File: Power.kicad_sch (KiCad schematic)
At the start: 49 parts, among them SW901 DP3T, U901 BQ24075, U902 TPS7A0533PDBV, U903 LP5907MFX-3.3

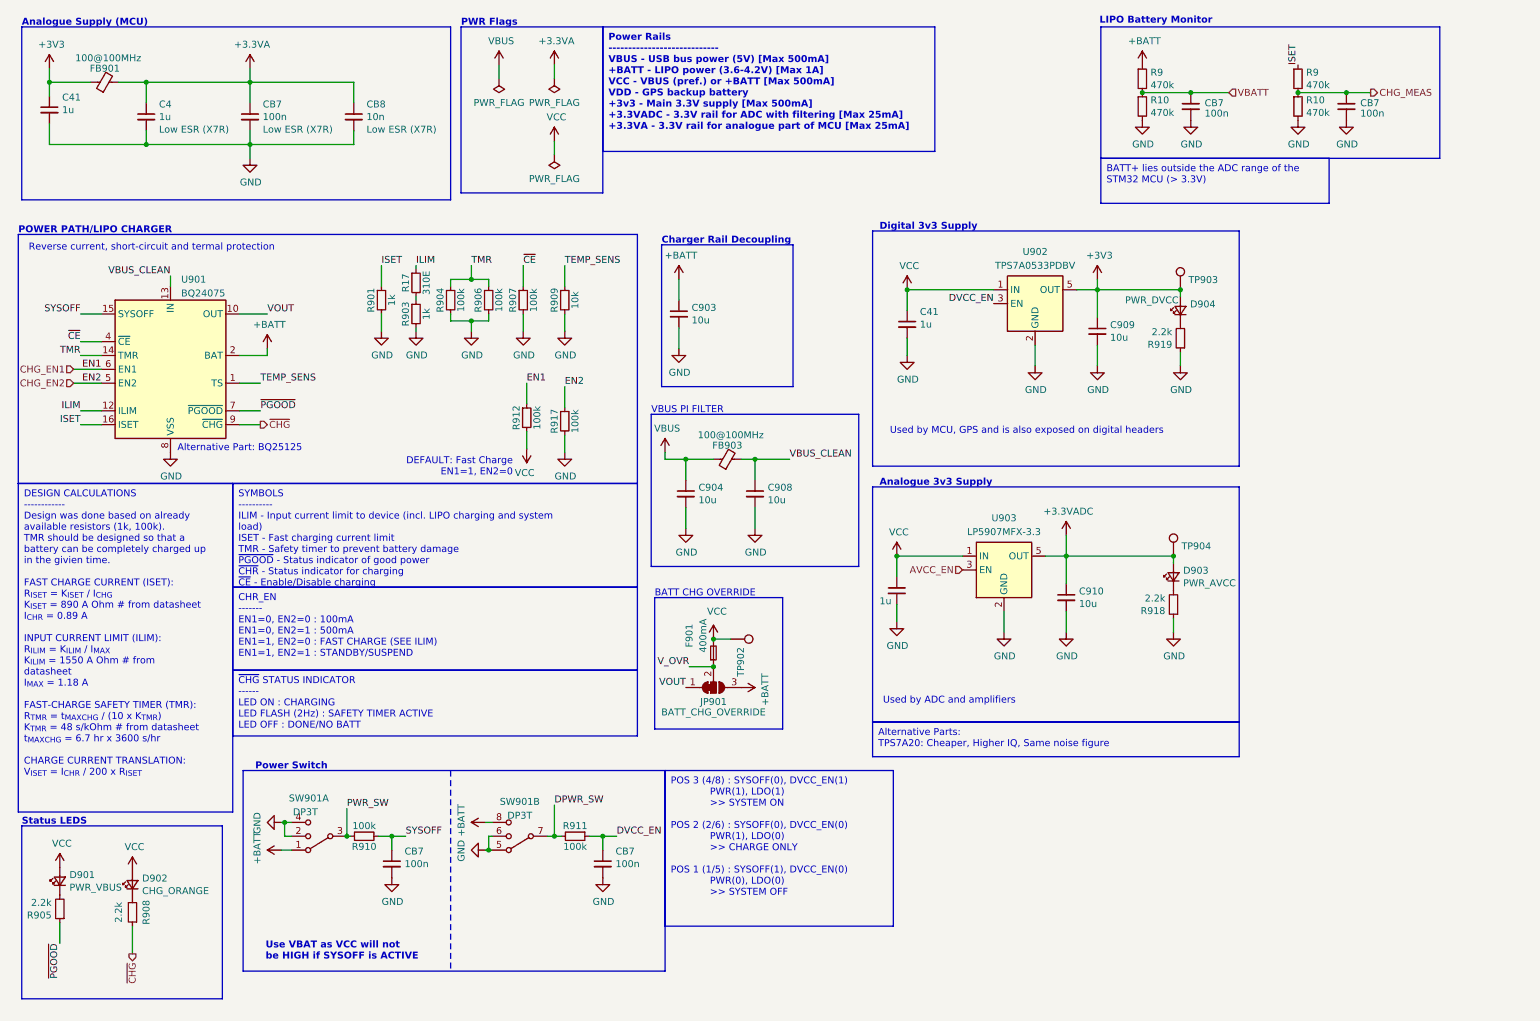
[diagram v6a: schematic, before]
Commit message: (sch) add analogue VCC load switch
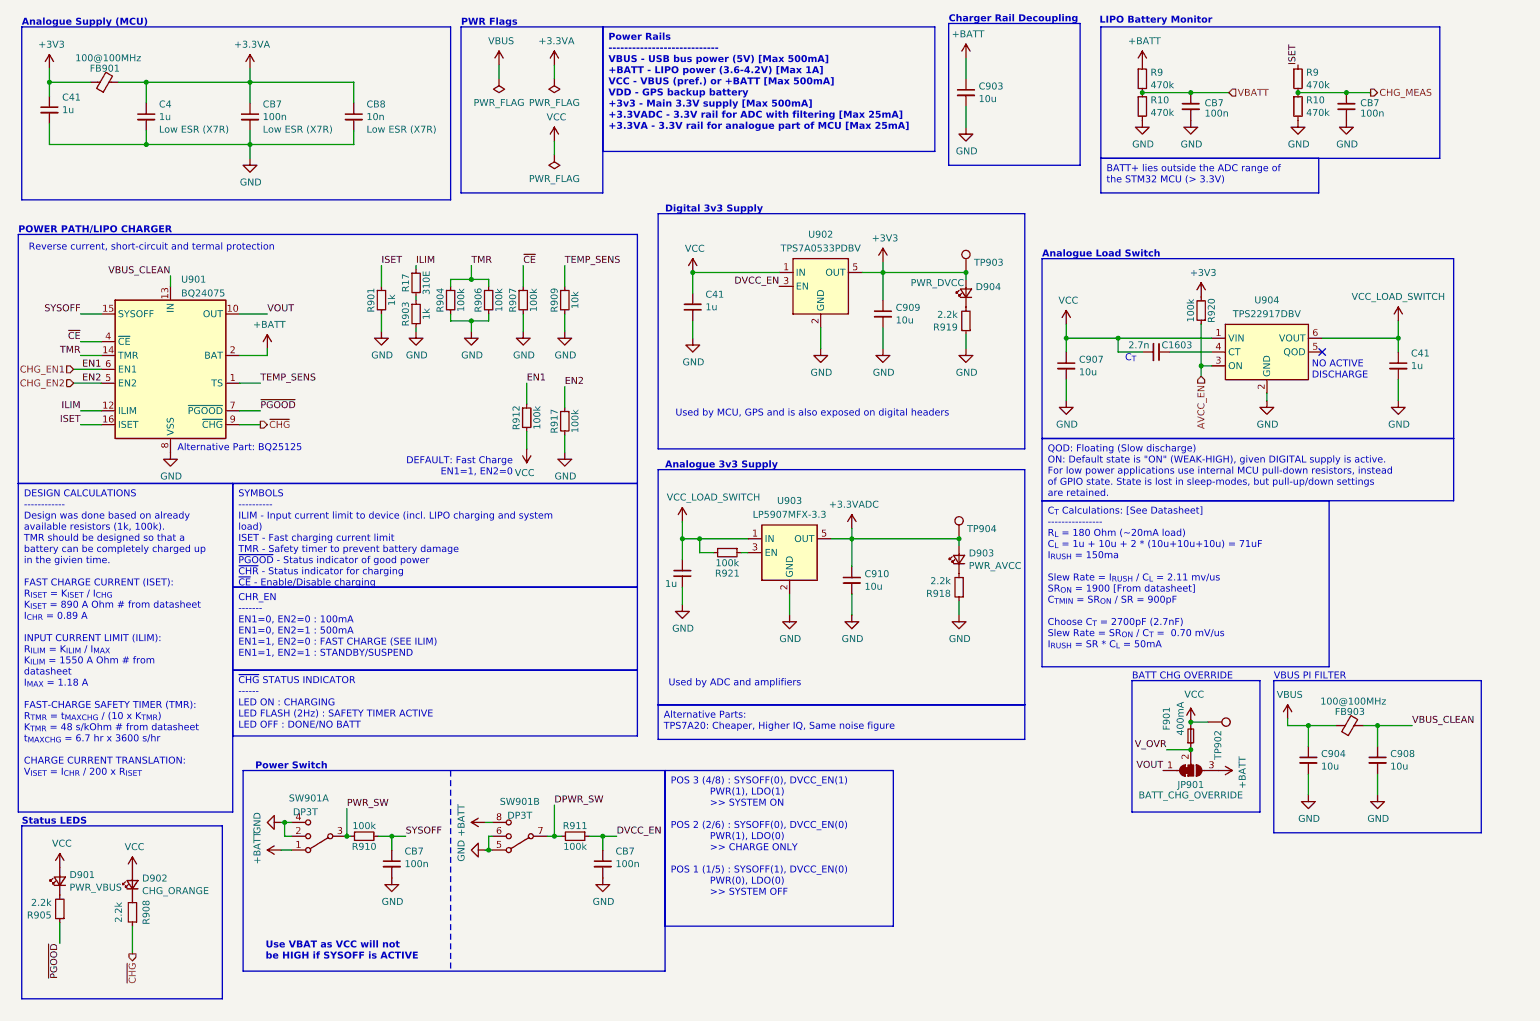
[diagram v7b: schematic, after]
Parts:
- added C1603: 2.7n, Capacitor_SMD:C_0402_1005Metric, symbol Device:C_Small
- added C41: 1u, Capacitor_SMD:C_0402_1005Metric, symbol Device:C_Small
- added C907: 10u, Capacitor_SMD:C_0402_1005Metric, symbol Device:C_Small
- added R920, R921: 100k, Resistor_SMD:R_0402_1005Metric, symbol Device:R_Small
- added U904: TPS22917DBV, Package_TO_SOT_SMD:SOT-23-6, symbol Power_Management:TPS22917DBV
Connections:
- net +3V3: now also R920.2
- net AVCC_EN: now also R920.1, U904.3 (ON); no longer U903.3 (EN)
- net GND: now also C41.2, C907.2, U904.2 (GND)
- net VCC: now also C1603.2, C907.1, U904.1 (VIN); no longer C41.1, U903.1 (IN)
- new net: C1603.1, U904.4 (CT)
- new net: R921.1, U903.3 (EN)
- new net VCC_LOAD_SWITCH: C41.1, C41.1, R921.2, U903.1 (IN), U904.6 (VOUT)
- no-connect marks 0 -> 1
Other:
- note added: "Analogue Load Switch"
- note added: "C_{T}"
- note added: "NO ACTIVE DISCHARGE"
- moved on the sheet: C41, C903, C904, C908, C909, C910, D903, D904, F901, FB903, JP901, R918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

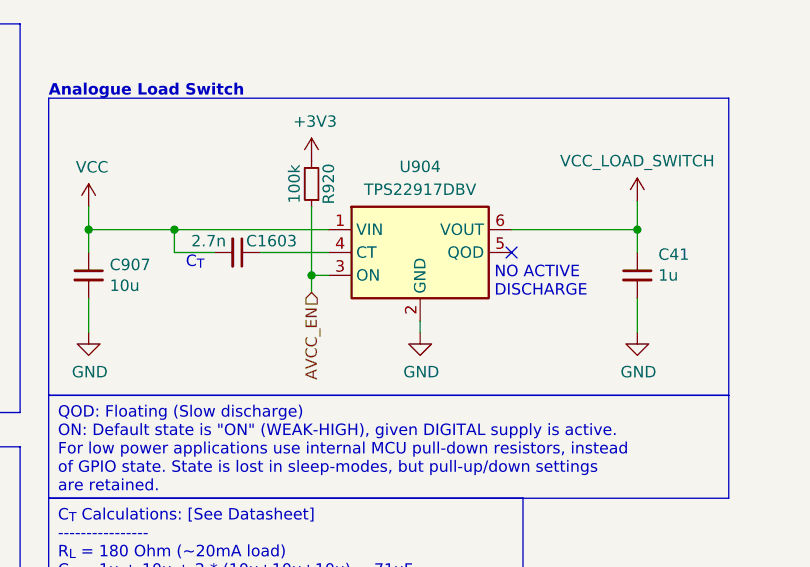
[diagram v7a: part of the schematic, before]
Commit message: (pcb) initial load switch layout
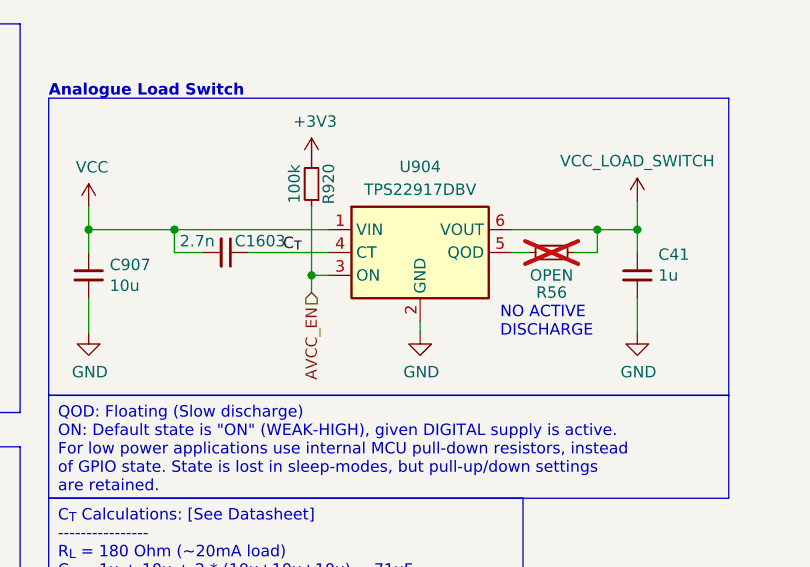
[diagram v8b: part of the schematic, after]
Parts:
- added R56: OPEN, Resistor_SMD:R_0402_1005Metric, symbol Device:R_Small
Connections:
- net VCC_LOAD_SWITCH: now also R56.2
- net C_{T}: now reaches C1603.1, U904.4 (CT)
- net at U904.5 (QOD): now also R56.1
- no-connect marks 1 -> 0
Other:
- note removed: "C_{T}"
- moved on the sheet: C1603
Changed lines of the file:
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@@
   (junction (at 267.97 73.66) (diameter 0) (color 0 0 0 0)
   )
+  (junction (at 263.525 73.66) (diameter 0) (color 0 0 0 0)
+  )
   (junction (at 121.92 165.1) (diameter 0) (color 0 0 0 0)
   )
@@
   (junction (at 139.7 110.49) (diameter 0) (color 0 0 0 0)
   )
-  (no_connect (at 254 76.2))
   (polyline (pts (xy 132.08 50.8) (xy 132.08 93.98))
     (stroke (width 0) (type default))
@@
     (stroke (width 0) (type default))
   )
-  (wire (pts (xy 226.06 76.2) (xy 233.68 76.2))
+  (wire (pts (xy 224.79 76.2) (xy 233.68 76.2))
     (stroke (width 0) (type default))
   )
@@
   )
   (wire (pts (xy 187.325 111.76) (xy 187.325 110.49))
+    (stroke (width 0) (type default))
+  )
+  (wire (pts (xy 254 76.2) (xy 255.905 76.2))
     (stroke (width 0) (type default))
   )
@@
     (stroke (width 0) (type default))
   )
-  (wire (pts (xy 220.98 76.2) (xy 216.535 76.2))
+  (wire (pts (xy 219.71 76.2) (xy 216.535 76.2))
     (stroke (width 0) (type default))
   )
@@
     (stroke (width 0) (type default))
   )
+  (wire (pts (xy 263.525 73.66) (xy 267.97 73.66))
+    (stroke (width 0) (type default))
+  )
+  (wire (pts (xy 260.985 76.2) (xy 263.525 76.2))
+    (stroke (width 0) (type default))
+  )
   (polyline (pts (xy 121.92 16.51) (xy 121.92 46.99))
     (stroke (width 0) (type default))
@@
     (stroke (width 0) (type default))
   )
+  (wire (pts (xy 263.525 76.2) (xy 263.525 73.66))
+    (stroke (width 0) (type default))
+  )
   (wire (pts (xy 136.525 110.49) (xy 139.7 110.49))
     (stroke (width 0) (type default))
@@
     (stroke (width 0) (type default))
   )
-  (wire (pts (xy 254 73.66) (xy 267.97 73.66))
+  (wire (pts (xy 254 73.66) (xy 263.525 73.66))
     (stroke (width 0) (type default))
   )
@@
   (text "Analogue Load Switch" (at 202.565 59.055 0)
     (effects (font (size 1.27 1.27) (thickness 0.254) bold) (justify left bottom))
-  )
-  (text "C_{T}" (at 217.805 78.105 0)
-    (effects (font (size 1.27 1.27)) (justify left bottom))
   )
   (text "Charger Rail Decoupling" (at 185.42 15.875 0)
@@
     (effects (font (size 1.27 1.27)) (justify left bottom))
   )
-  (text "NO ACTIVE\nDISCHARGE" (at 252.095 81.28 0)
+  (text "NO ACTIVE\nDISCHARGE" (at 252.73 85.725 0)
     (effects (font (size 1.27 1.27)) (justify left bottom))
   )
@@
     (effects (font (size 1.27 1.27)) (justify left bottom))
   )
+  (label "C_{T}" (at 228.6 76.2 0) (fields_autoplaced)
+    (effects (font (size 1.27 1.27)) (justify left bottom))
+  )
   (label "ILIM" (at 87.63 60.325 0) (fields_autoplaced)
     (effects (font (size 1.27 1.27)) (justify left bottom))
@@
         (path "/4185c36c-c66e-4dbd-be5d-841e551f4885/00000000-0000-0000-0000-00005eede770"
           (reference "U902") (unit 1)
+        )
+      )
+    )
+  )
+  (symbol (lib_id "Device:R_Small") (at 258.445 76.2 90) (unit 1)
+    (in_bom no) (on_board yes) (dnp yes)
+    (property "Reference" "R56" (at 258.445 80.645 90)
+      (effects (font (size 1.27 1.27)))
+    )
+    (property "Value" "OPEN" (at 258.445 78.74 90)
+      (effects (font (size 1.27 1.27)))
+    )
+    (property "Footprint" "Resistor_SMD:R_0402_1005Metric" (at 258.445 76.2 0)
+      (effects (font (size 1.27 1.27)) hide)
+    )
+    (property "Datasheet" "~" (at 258.445 76.2 0)
+      (effects (font (size 1.27 1.27)) hide)
+    )
+    (property "MPN" "DNP" (at 258.445 76.2 0)
+      (effects (font (size 1.27 1.27)) hide)
+    )
+    (property "Mfr." "DNP" (at 258.445 76.2 0)
+      (effects (font (size 1.27 1.27)) hide)
+    )
+    (pin "1")
+    (pin "2")
+    (instances
+      (project "kleinvoet"
+        (path "/4185c36c-c66e-4dbd-be5d-841e551f4885/00000000-0000-0000-0000-00005ee5ecad/00000000-0000-0000-0000-00005ee62baf"
+          (reference "R56") (unit 1)
+        )
+        (path "/4185c36c-c66e-4dbd-be5d-841e551f4885/00000000-0000-0000-0000-00005ee5ecad/00000000-0000-0000-0000-00005ee91c90"
+          (reference "R57") (unit 1)
+        )
+        (path "/4185c36c-c66e-4dbd-be5d-841e551f4885/00000000-0000-0000-0000-00005ee5ecad/00000000-0000-0000-0000-00005ee62c2b"
+          (reference "R501") (unit 1)
+        )
+        (path "/4185c36c-c66e-4dbd-be5d-841e551f4885/00000000-0000-0000-0000-00005ee5ecad/f1c168a4-8e09-4be7-8226-fa7de49180b9"
+          (reference "R601") (unit 1)
+        )
+        (path "/4185c36c-c66e-4dbd-be5d-841e551f4885/b53619ea-788f-4bc9-9946-594014d7d22c/7d55f5f7-ad99-481b-88b5-315ad3d2b07e"
+          (reference "R1101") (unit 1)
+        )
+        (path "/4185c36c-c66e-4dbd-be5d-841e551f4885/00000000-0000-0000-0000-00005eede770"
+          (reference "R922") (unit 1)
         )
       )
@@
     )
   )
-  (symbol (lib_id "Device:C_Small") (at 223.52 76.2 270) (unit 1)
-    (in_bom yes) (on_board yes) (dnp no)
-    (property "Reference" "C1603" (at 227.33 74.93 90)
-      (effects (font (size 1.27 1.27)))
-    )
-    (property "Value" "2.7n" (at 220.345 74.93 90)
-      (effects (font (size 1.27 1.27)))
-    )
-    (property "Footprint" "Capacitor_SMD:C_0402_1005Metric" (at 223.52 76.2 0)
-      (effects (font (size 1.27 1.27)) hide)
-    )
-    (property "Datasheet" "~" (at 223.52 76.2 0)
-      (effects (font (size 1.27 1.27)) hide)
-    )
-    (property "MPN" "GRM1555C1H272GE01D" (at 223.52 76.2 0)
-      (effects (font (size 1.27 1.27)) hide)
-    )
-    (property "Mfr." "Murata" (at 223.52 76.2 0)
-      (effects (font (size 1.27 1.27)) hide)
-    )
+  (symbol (lib_id "Device:C_Small") (at 222.25 76.2 270) (unit 1)
+    (in_bom yes) (on_board yes) (dnp no)
+    (property "Reference" "C1603" (at 226.06 74.93 90)
+      (effects (font (size 1.27 1.27)))
+    )
+    (property "Value" "2.7n" (at 219.075 74.93 90)
+      (effects (font (size 1.27 1.27)))
+    )
+    (property "Footprint" "Capacitor_SMD:C_0402_1005Metric" (at 222.25 76.2 0)
+      (effects (font (size 1.27 1.27)) hide)
+    )
+    (property "Datasheet" "~" (at 222.25 76.2 0)
+      (effects (font (size 1.27 1.27)) hide)
+    )
+    (property "MPN" "GRM1555C1H272GE01D" (at 222.25 76.2 0)
+      (effects (font (size 1.27 1.27)) hide)
+    )
+    (property "Mfr." "Murata" (at 222.25 76.2 0)
+      (effects (font (size 1.27 1.27)) hide)
+    )
